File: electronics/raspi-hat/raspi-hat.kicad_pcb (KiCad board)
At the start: 4 copper layers, 65 x 56 mm, 29 parts, among them J1 12V from battery, J2 5V to other boards, J3 40HAT, J4 CAN, Q1 DMG2305UX, Q2 DMMT5401, U1 MCP2515-xSO, U2 LD3985M33R_SOT23, U3 MAX33012EASA+, U4 MYMGA5R04RELA5RA, Y1 8MHz

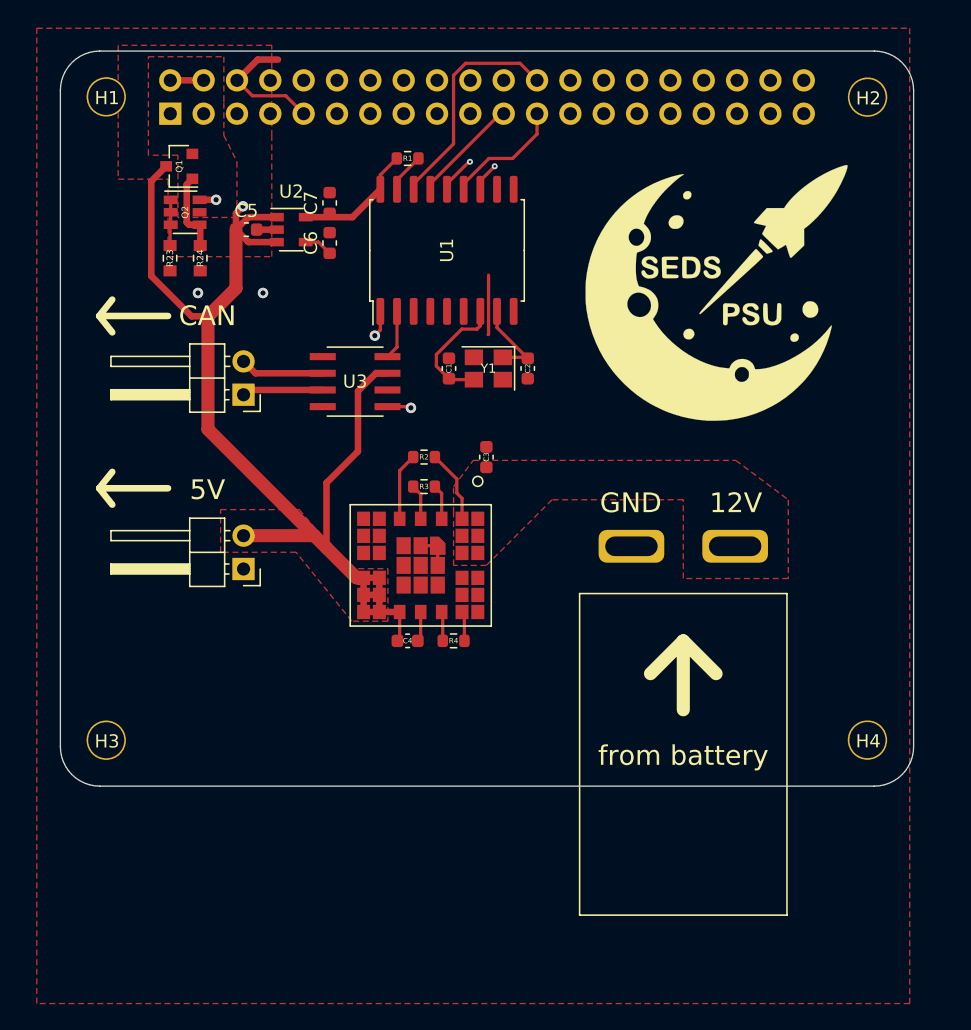
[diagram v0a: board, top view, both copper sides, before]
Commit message: Update Raspberry Pi HAT to Rev 2 requirements
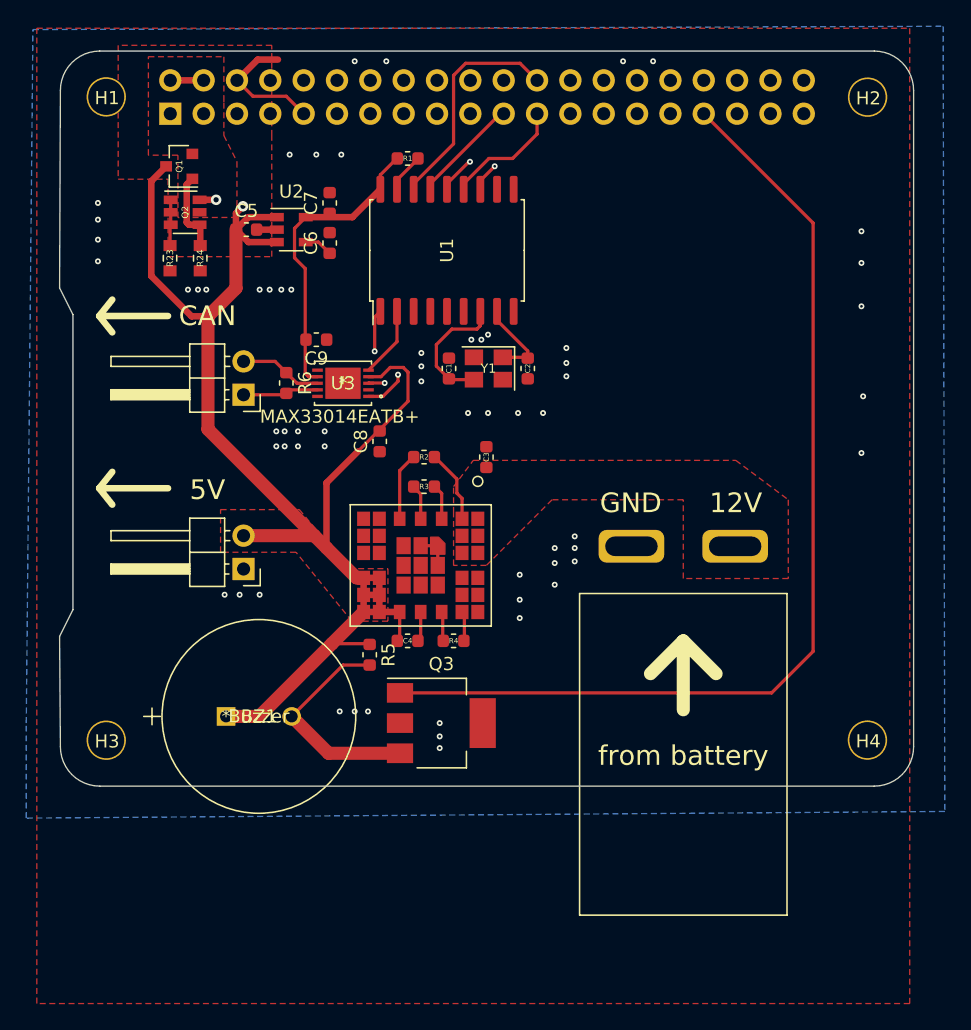
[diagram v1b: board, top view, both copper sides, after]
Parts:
- removed Ref**: Val**, Custom Footprints:seds-logo
- added BZ1: Buzzer, PS1420P02CT:PS1420P02CT, F.Cu at (91.2, 111.5)
- added C8: 0.1uF, Capacitor_SMD:C_0603_1608Metric, F.Cu at (102.9, 90.6)
- added C9: 0.1uF, Capacitor_SMD:C_0603_1608Metric, F.Cu at (98.0, 82.8)
- added Q3: Q_NMOS_GSD, Package_TO_SOT_SMD:SOT-223, F.Cu at (107.6, 112.0)
- added R5: 1k, Resistor_SMD:R_0603_1608Metric, F.Cu at (102.1, 106.8)
- added R6: 120, Resistor_SMD:R_0603_1608Metric, F.Cu at (95.8, 86.1)
- U3: value MAX33012EASA+ -> MAX33014EATB+; footprint MAX33012EASA+:MAX33012EASA+ -> MAX33014E:MAX33014EATB&plus_
- moved U3 0.93 mm to (100.1, 86.1)
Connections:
- J3 pad 33: unconnected-(J3-Pad33) -> /BUZZER_CTRL
- U3 pad 2: GND -> unconnected-(U3-Pad2)
- U3 pad 3: +5V -> GND
- U3 pad 4: Net-(U1-Pad2) -> +5V
- U3 pad 5: unconnected-(U3-Pad5) -> Net-(U1-Pad2)
- U3 pad 6: Net-(J4-Pad2) -> unconnected-(U3-Pad6)
- U3 pad 7: Net-(J4-Pad1) -> +3V3
- U3 pad 8: unconnected-(U3-Pad8) -> Net-(J4-Pad2)
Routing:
- net /BUZZER_CTRL: track 0.00 -> 77.2 mm
- net +5V: track 93.3 -> 113.7 mm
- net Net-(BZ1-Pad2): track 0.00 -> 17.0 mm
- net +3V3: track 9.43 -> 23.1 mm
- net GND: track 28.3 -> 20.1 mm, vias 2 -> 63
- net Net-(U1-Pad1): track 11.8 -> 8.97 mm
- net Net-(U1-Pad2): track 3.75 -> 5.38 mm
- added copper zone on B.Cu, net GND
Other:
- board size 65 x 56 mm -> 65.1 x 56 mm

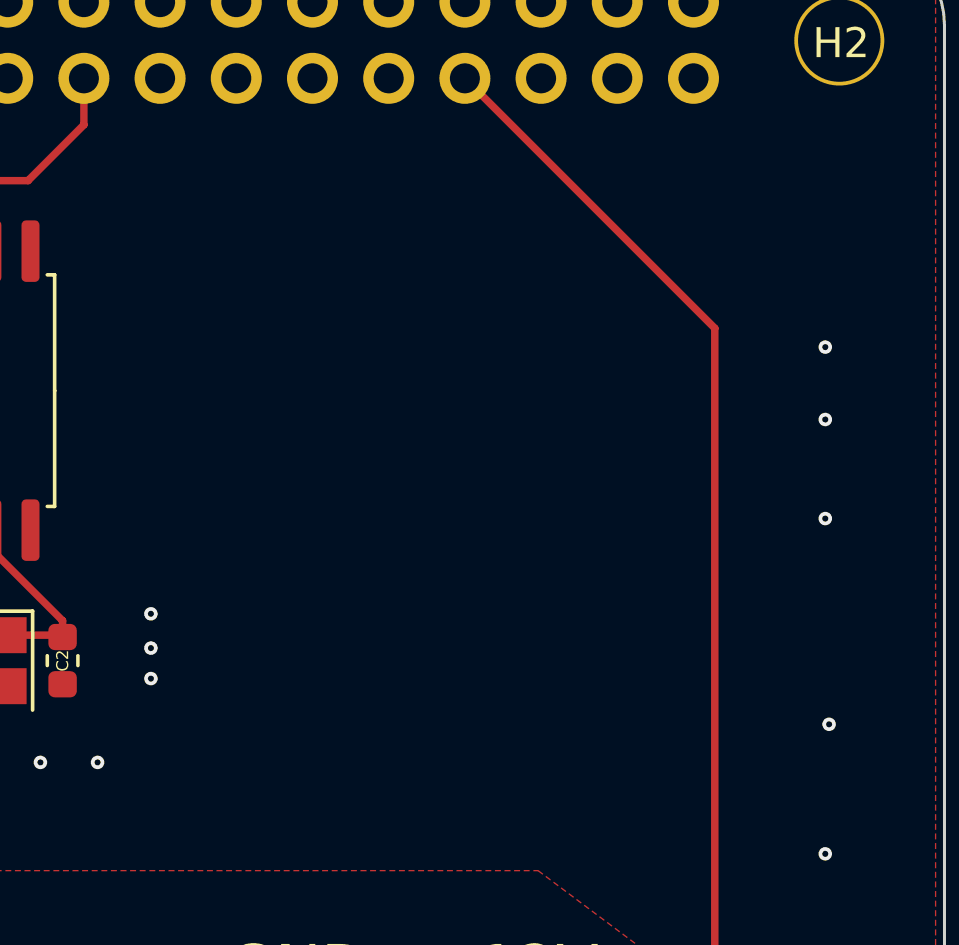
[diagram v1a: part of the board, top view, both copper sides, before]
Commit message: Re-add SEDS logo to Raspberry Pi HAT
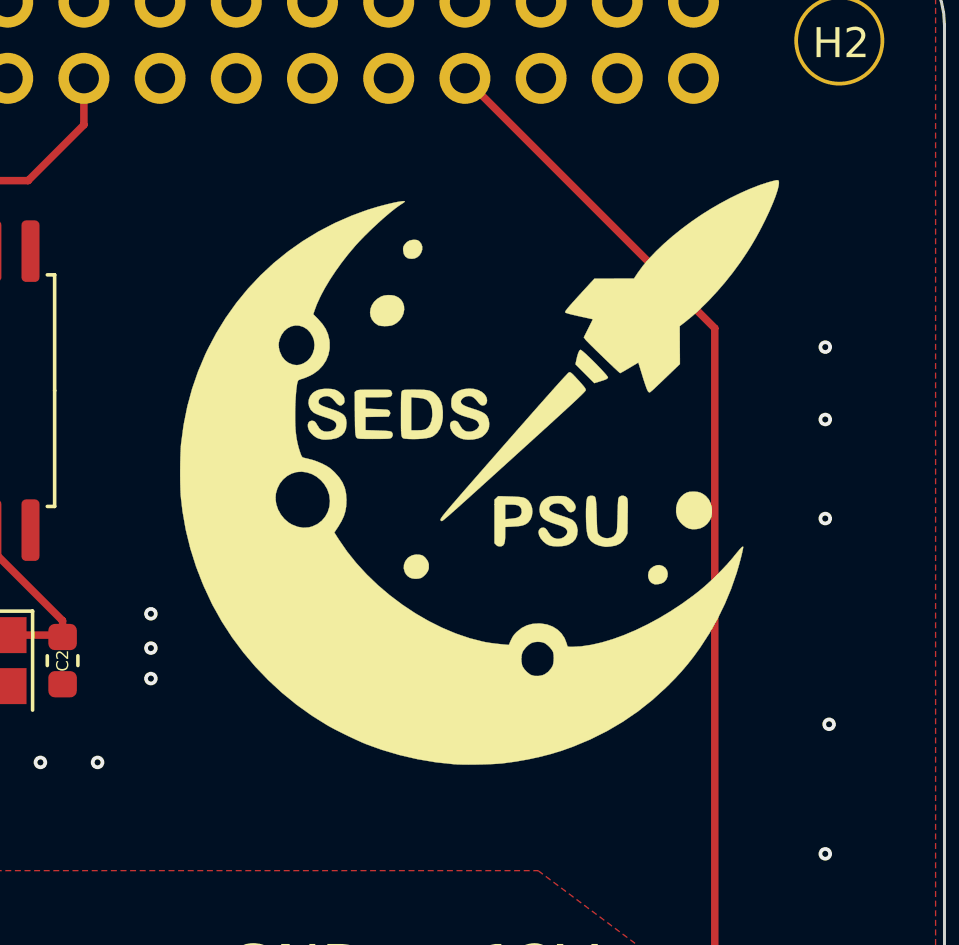
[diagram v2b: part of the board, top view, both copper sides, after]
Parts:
- added Ref**: Val**, Custom Footprints:seds-logo, F.Cu at (128.0, 78.5)

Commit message: Update HAT
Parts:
- Q3: footprint Package_TO_SOT_SMD:SOT-223 -> Package_TO_SOT_SMD:SOT-23
- moved Q3 3.31 mm to (104.8, 110.2), turned to 180 degrees
- moved Ref** 0.40 mm to (128.4, 78.6)
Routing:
- net GND: track 20.1 -> 10.1 mm, vias 63 -> 70
- net Net-(BZ1-Pad2): track 17.0 -> 10.9 mm
- net +3V3: track 23.1 -> 24.0 mm
- net /BUZZER_CTRL: track 77.2 -> 76.4 mm
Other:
- board size 65.1 x 56 mm -> 65.1 x 58.7 mm

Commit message: Fix unconnected items
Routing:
- net GND: vias 70 -> 73
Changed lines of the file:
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@@
   (via (at 117.094 85.598) (size 0.45) (drill 0.2) (layers "F.Cu" "B.Cu") (free) (net 1))
   (via (at 99.949 96.266) (size 0.45) (drill 0.2) (layers "F.Cu" "B.Cu") (free) (net 1))
+  (via (at 100.584 83.058) (size 0.45) (drill 0.2) (layers "F.Cu" "B.Cu") (free) (net 1))
   (via (at 88.265 78.994) (size 0.45) (drill 0.2) (layers "F.Cu" "B.Cu") (free) (net 1))
   (via (at 99.949 97.028) (size 0.45) (drill 0.2) (layers "F.Cu" "B.Cu") (free) (net 1))
@@
   (via (at 117.729 97.79) (size 0.45) (drill 0.2) (layers "F.Cu" "B.Cu") (free) (net 1))
   (via (at 113.411 88.392) (size 0.45) (drill 0.2) (layers "F.Cu" "B.Cu") (free) (net 1))
+  (via (at 100.584 82.169) (size 0.45) (drill 0.2) (layers "F.Cu" "B.Cu") (free) (net 1))
   (via (at 96.139 74.422) (size 0.45) (drill 0.2) (layers "F.Cu" "B.Cu") (free) (net 1))
   (via (at 139.573 76.962) (size 0.45) (drill 0.2) (layers "F.Cu" "B.Cu") (free) (net 1))
   (via (at 103.251 86.106) (size 0.45) (drill 0.2) (layers "F.Cu" "B.Cu") (free) (net 1))
   (via (at 111.125 82.423) (size 0.45) (drill 0.2) (layers "F.Cu" "B.Cu") (free) (net 1))
+  (via (at 100.584 81.28) (size 0.45) (drill 0.2) (layers "F.Cu" "B.Cu") (free) (net 1))
   (via (at 116.205 98.679) (size 0.45) (drill 0.2) (layers "F.Cu" "B.Cu") (free) (net 1))
   (via (at 109.601 88.392) (size 0.45) (drill 0.2) (layers "F.Cu" "B.Cu") (free) (net 1))

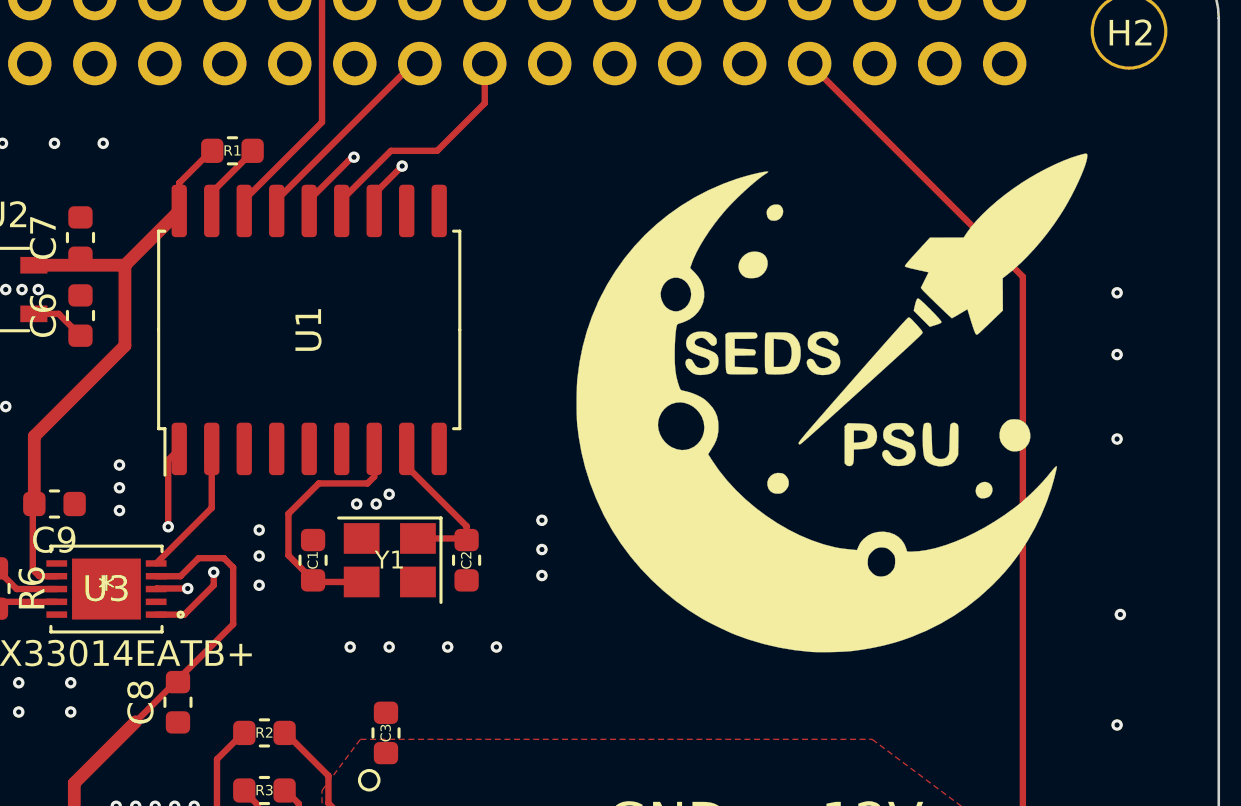
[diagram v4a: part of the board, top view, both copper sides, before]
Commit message: Fix DRC errors on Raspi HAT
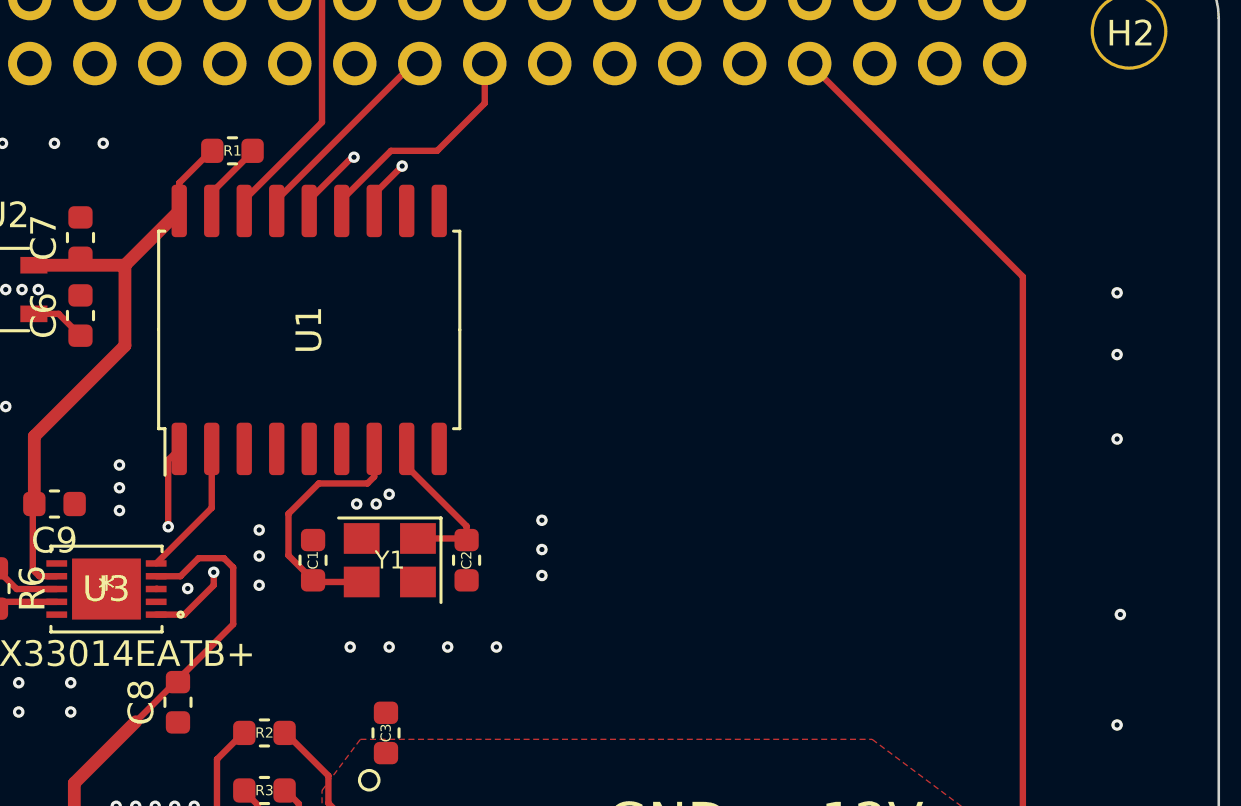
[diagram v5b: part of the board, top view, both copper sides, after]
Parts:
- removed Ref**: Val**, Custom Footprints:seds-logo
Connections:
- U3 pad 2: unconnected-(U3-Pad2) -> GND
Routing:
- net GND: track 10.1 -> 8.94 mm
